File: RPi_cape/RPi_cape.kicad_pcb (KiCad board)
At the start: 4 copper layers, 104 x 255 mm, 505 parts, among them J1 Conn_01x04, J10 Conn_01x02, J11 Conn_01x02, J12 Conn_01x02, J13 Conn_01x02, J14 Conn_01x02, J16 Conn_01x06, J17 Pressure_sensor_barb, J18 Pressure_sensor_barb, J19 Pressure_sensor_barb, J2 Conn_01x02, J20 Pressure_sensor_barb, J3 Conn_01x02, J4 Conn_01x02, J5 Conn_01x03, J6 Conn_01x03, J7 Conn_01x02, J8 Conn_02x20_Odd_Even, J9 Conn_01x02, P15 Conn_02x05_Odd_Even, Q1 MMBT3904, Q10 MMBT3904, Q11 MMBT3904, Q12 MMBT3906, Q13 MMBT3904, Q5 MMBT3904, Q6 DNP, Q7 DNP, Q8 MMBT3904, Q9 MMBT3904, U1 TL431A, U10 MS5803-05BA, U11 LM2903, U12 LMC7101B, U13 LMC7101B, U14 BMP388, U15 MS5803-05BA, U16 BMP388, U17 LM2903, U18 74LVC1G08, U19 TPS1H100B, U2 ADC128D818, U20 74LVC1G08, U21 TPS1H100B, U22 74LVC1G08, U23 TPS1H100B, U24 TL431A, U25 LM2903, U26 MIC1557, U27 MIC1557, U28 LM4871M, U29 LP5907MFX-3.3, U3 ADC128D818, U30 LP5907MFX-1.8, U31 DNP (5M40ZE64), U32 MIC1557, U33 5M80ZT100 / 5M240ZT100, U34 LMZ14203, U35 LMZ14203, U36 LMC7101B, U37 LMC7101B, U38 LMC7101B, U4 AD8552A, U5 LM2903, U6 LMC7101B, U7 LMC7101B, U8 74LVC1G08, U9 TPS1H100B

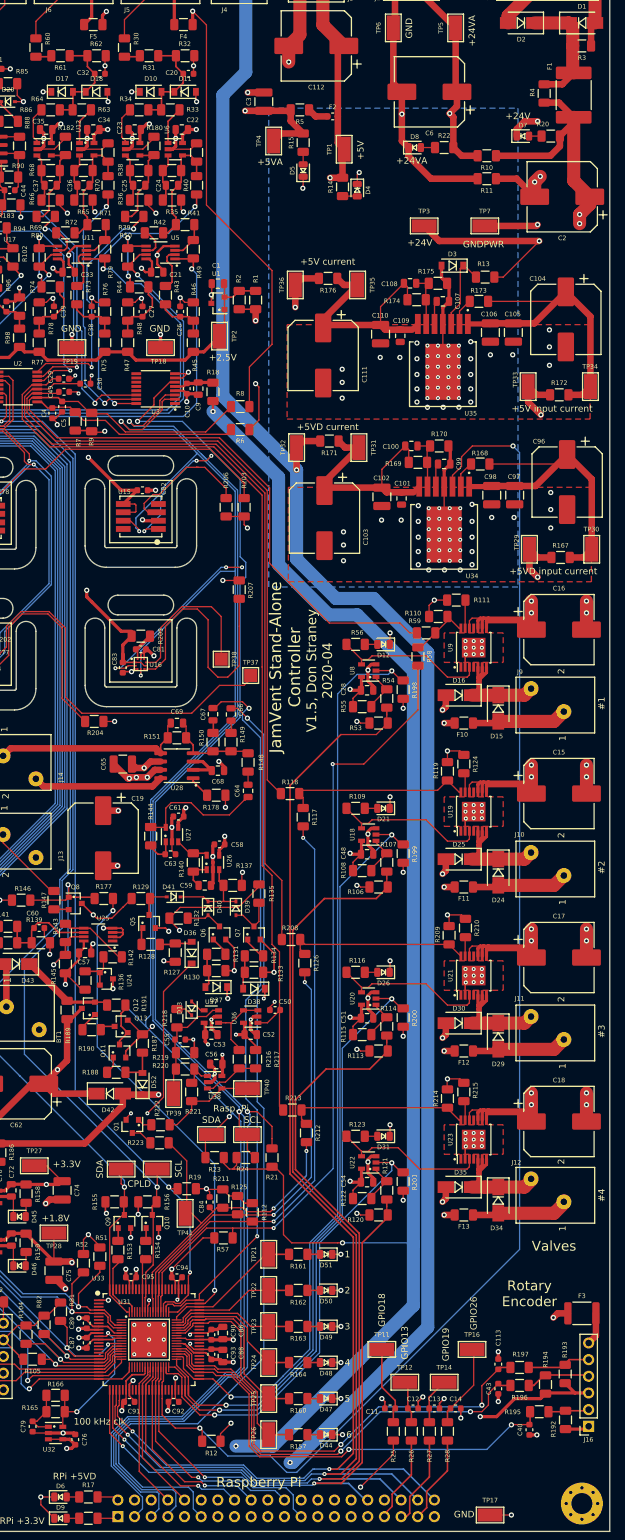
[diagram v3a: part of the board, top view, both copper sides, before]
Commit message: Safety additions
Switched CPLD_ADC7 to +24V monitoring (from +5V monitoring), and added CPLD ~Bat_On digital input(s) to know when it's running from backup battery, to cover low-input-voltage edge cases
Added series 1K resistors (R226-231) on CPLD<->RPi Comms1-6 lines, to protect CPLD in case of overvoltage from RPi failure
Added optional input TVS D23 to handle sustained over-voltage or large surges
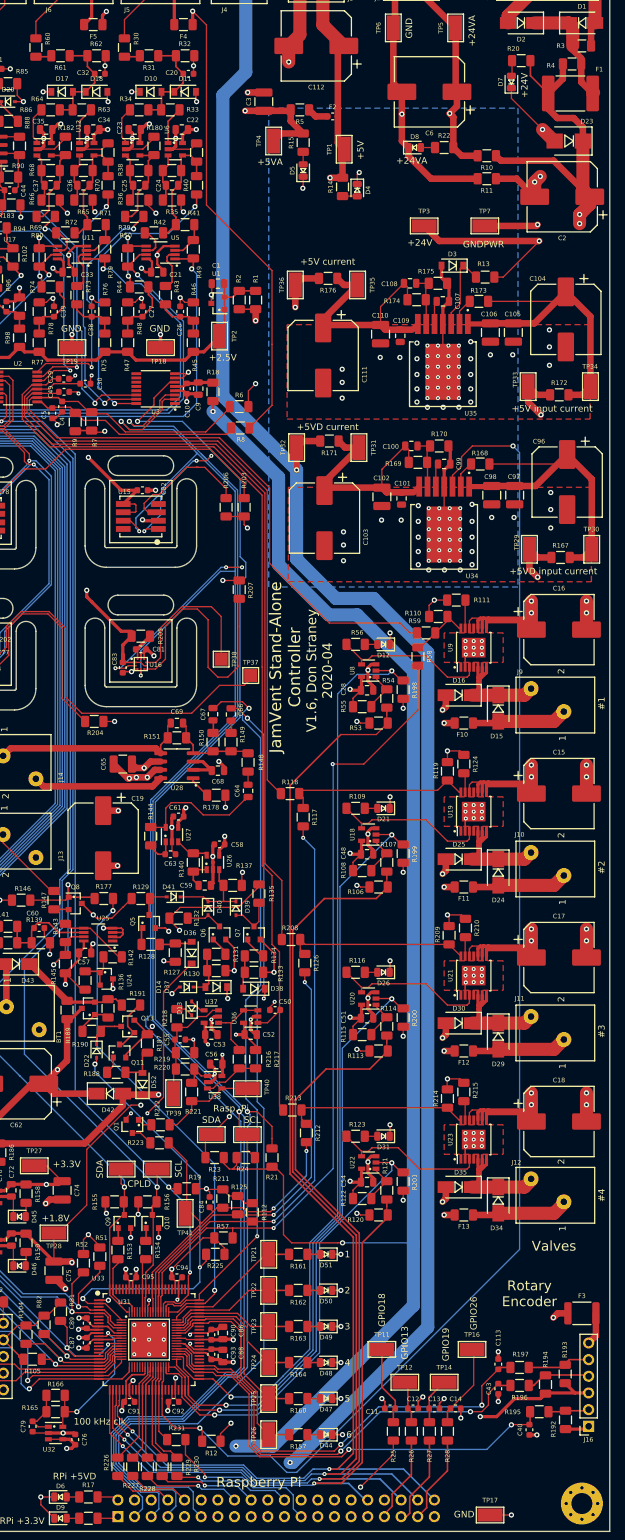
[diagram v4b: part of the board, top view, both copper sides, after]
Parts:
- added D14: BAS21AH, Ventilator:D_SOD-323, F.Cu at (68.0, 200.5)
- added D22: BAS21AH, Ventilator:D_SOD-323, F.Cu at (54.2, 210.2)
- added D23: DNP, Ventilator:D_SMB, F.Cu at (126.2, 71.5)
- added R224: 10K, Resistor_SMD:R_1206_3216Metric, F.Cu at (56.0, 203.8)
- added R225: 10K, Resistor_SMD:R_1206_3216Metric, F.Cu at (72.3, 241.2)
- added R226: 1K, Resistor_SMD:R_1206_3216Metric, F.Cu at (57.5, 273.6)
- added R227: 1K, Resistor_SMD:R_1206_3216Metric, F.Cu at (59.8, 273.6)
- added R228: 1K, Resistor_SMD:R_1206_3216Metric, F.Cu at (62.0, 273.6)
- added R229: 1K, Resistor_SMD:R_1206_3216Metric, F.Cu at (64.2, 273.6)
- added R230: 1K, Resistor_SMD:R_1206_3216Metric, F.Cu at (66.5, 273.6)
- added R231: 1K, Resistor_SMD:R_1206_3216Metric, F.Cu at (66.4, 269.5)
- D37: value 3.3V -> DNP (3.3V)
- D38: value 20V -> DNP (20V)
- D39: value BAS21AH -> DNP (BAS21AH)
- Q6: value DNP -> MMBT3904
- R130, R9: value DNP -> 1K
- R131, R132, R8: value DNP -> 10K
- R6, R7: value 10K -> DNP (10K)
- moved R20 12.3 mm to (119.0, 59.2)
- moved D7 8.43 mm to (117.5, 62.5), turned to 90 degrees
- moved R4 6.19 mm to (126.8, 59.8), turned to 180 degrees
- moved R6 3.50 mm to (76.0, 112.0)
- moved R8 3.25 mm to (76.2, 115.2)
- moved R7 2.50 mm to (53.5, 114.2)
- moved R9 2.50 mm to (51.0, 114.3)
- moved R191 2.25 mm to (59.5, 203.2)
- moved C4 1.80 mm to (49.0, 112.0)
- moved C5 1.80 mm to (47.5, 113.0)
- moved Q13 1.00 mm to (59.0, 206.5)
- moved R187 0.75 mm to (62.0, 209.1)
- moved F1 0.56 mm to (126.5, 64.2), turned to 0 degrees
- moved R190 0.25 mm to (53.5, 207.2)
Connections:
- C4 pad 2: /CPLD_ADC7 -> /CPLD_ADC6
- C5 pad 2: /CPLD_ADC6 -> /CPLD_ADC7
- R6 pad 2: /CPLD_ADC7 -> /CPLD_ADC6
- R7 pad 1: /CPLD_ADC7 -> /CPLD_ADC6
- R8 pad 2: /CPLD_ADC6 -> /CPLD_ADC7
- R9 pad 1: /CPLD_ADC6 -> /CPLD_ADC7
- U31 pad 1: Net-(U31-Pad1) -> /Auditory Alarm/~Bat_On
- U31 pad 24: /Comms1 -> /CPLD/Comms1
- U31 pad 25: /Comms2 -> /CPLD/Comms2
- U31 pad 26: /Comms3 -> /CPLD/Comms3
- U31 pad 27: /Comms4 -> /CPLD/Comms4
- U31 pad 28: /Comms5 -> /CPLD/Comms5
- U31 pad 29: /Comms6 -> /CPLD/Comms6
- U33 pad 2: Net-(U33-Pad2) -> /Auditory Alarm/~Bat_On
- U33 pad 35: /Comms1 -> /CPLD/Comms1
- U33 pad 36: /Comms2 -> /CPLD/Comms2
- U33 pad 37: /Comms3 -> /CPLD/Comms3
- U33 pad 39: /Comms4 -> /CPLD/Comms4
- U33 pad 40: /Comms5 -> /CPLD/Comms5
- U33 pad 41: /Comms6 -> /CPLD/Comms6
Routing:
- net /Auditory Alarm/~Bat_On: track 0.00 -> 70.0 mm, vias 0 -> 3
- net +1V8: track 72.4 -> 120.1 mm, vias 3 -> 5
- net /Comms5: track 34.8 -> 17.9 mm
- net /Comms4: track 31.0 -> 15.1 mm
- net /CPLD/Comms5: track 0.00 -> 15.9 mm
- net /CPLD/Comms1: track 0.00 -> 15.7 mm
- net +24V: track 225.0 -> 240.7 mm
- net /Comms3: track 29.9 -> 14.8 mm
- net /CPLD/Comms2: track 0.00 -> 14.9 mm
- net /CPLD/Comms4: track 0.00 -> 14.6 mm
- net /CPLD/Comms3: track 0.00 -> 14.4 mm
- net /Comms2: track 23.4 -> 9.48 mm
- net /Comms1: track 22.6 -> 9.14 mm
- net /Comms6: track 38.2 -> 25.4 mm
- net /CPLD/Comms6: track 0.00 -> 11.7 mm
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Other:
- board text added: "V1.6, Don Straney 2020-04"
- board text removed: "V1.5, Don Straney 2020-04"

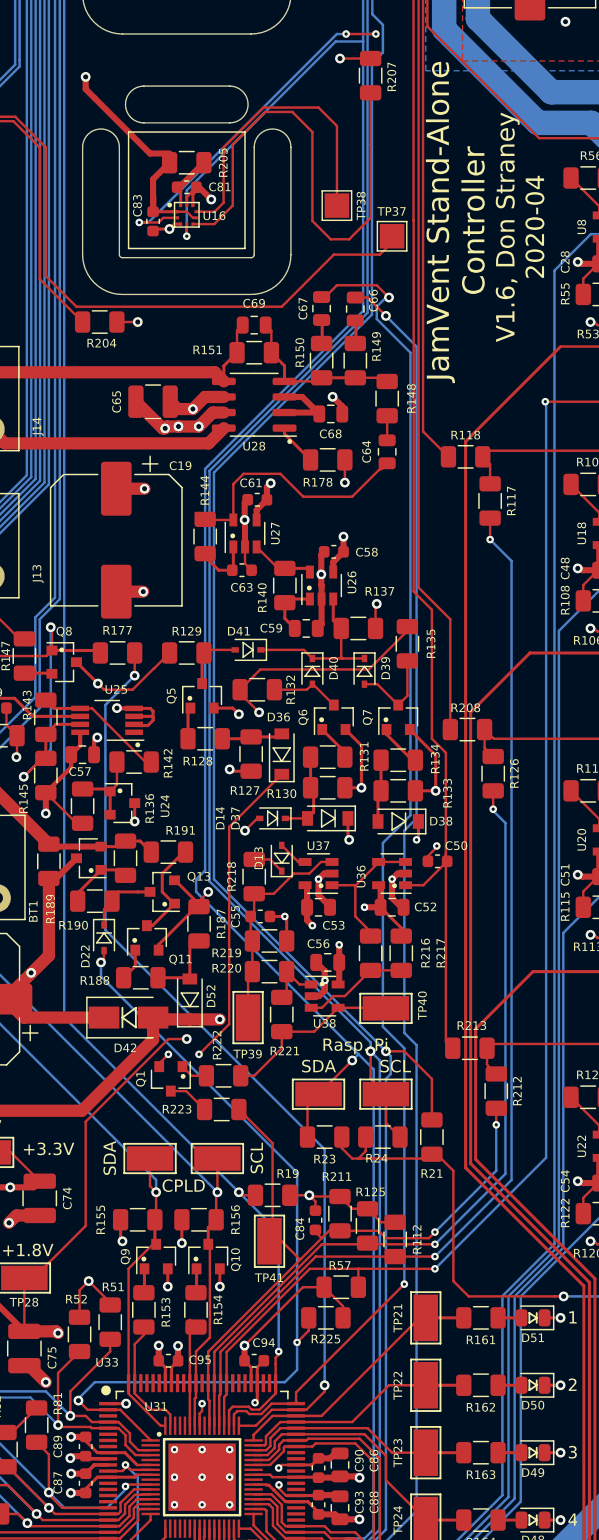
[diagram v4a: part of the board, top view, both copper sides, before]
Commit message: +5VA outage detection
Separated +1.8V and +5VA monitoring and added +3.3V output for +5VA on ~5VA_On signal to CPLD, to cover an extra failure mode
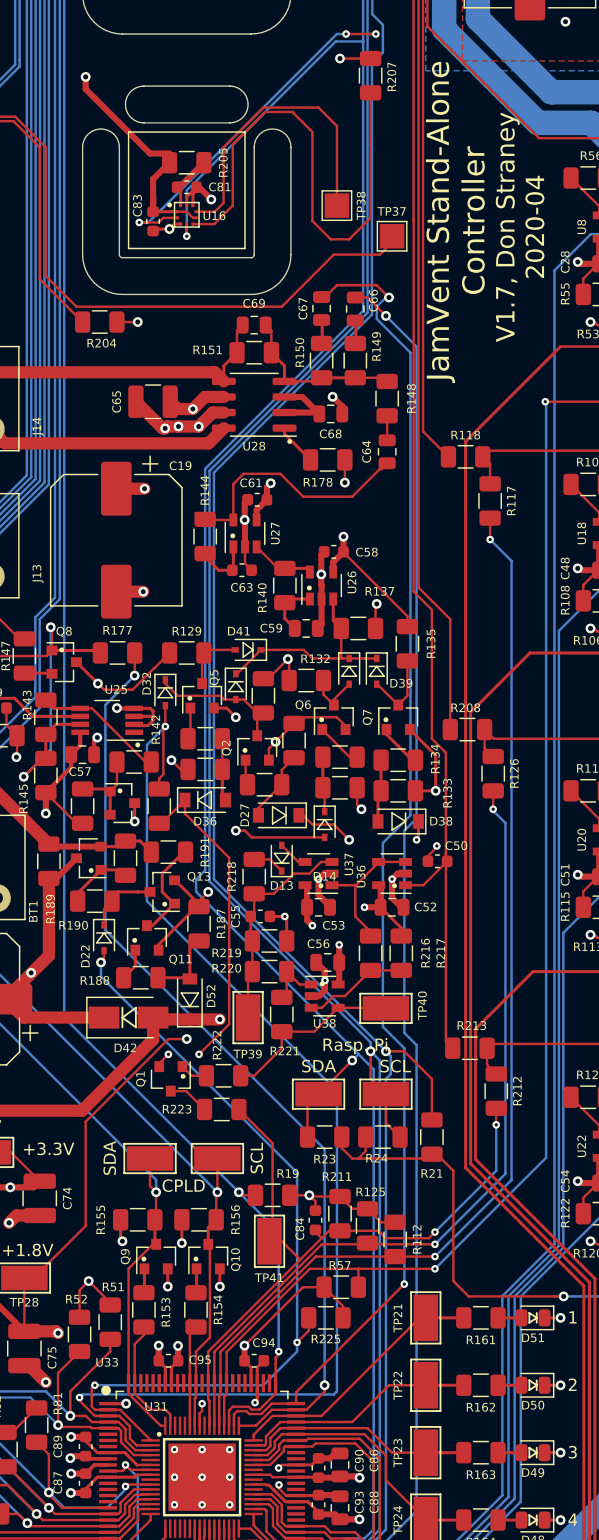
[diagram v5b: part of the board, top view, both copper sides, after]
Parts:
- removed D37: DNP (3.3V), Ventilator:D_SOD-123
- added D27: 3.3V, Ventilator:D_SOD-123, F.Cu at (68.5, 200.2)
- added D28: DNP (BAS21AH), Ventilator:D_SOD-323, F.Cu at (65.0, 189.8)
- added D32: BAS21AH, Ventilator:D_SOD-323, F.Cu at (59.2, 190.2)
- added Q2: MMBT3904, Ventilator:SOT-23, F.Cu at (66.8, 194.8)
- added R232: 10K, Resistor_SMD:R_1206_3216Metric, F.Cu at (69.8, 194.2)
- added R233: 10K, Resistor_SMD:R_1206_3216Metric, F.Cu at (67.3, 197.8)
- added R234: 10K, Resistor_SMD:R_1206_3216Metric, F.Cu at (67.2, 190.5)
- added R235: 10K, Resistor_SMD:R_1206_3216Metric, F.Cu at (58.8, 199.5)
- moved D36 7.29 mm to (62.5, 199.0), turned to 0 degrees
- moved D14 4.28 mm to (72.2, 201.0), turned to 270 degrees
- moved R132 4.07 mm to (70.8, 189.2)
- moved R127 3.95 mm to (62.5, 196.5), turned to 0 degrees
- moved D40 3.00 mm to (74.2, 188.5)
- moved D39 1.00 mm to (76.5, 188.5)
- moved R130 1.00 mm to (73.5, 198.0)
- moved R131 1.00 mm to (73.5, 195.5)
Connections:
- U31 pad 2: Net-(U31-Pad2) -> /Auditory Alarm/~+5VA_On
- U33 pad 3: Net-(U33-Pad3) -> /Auditory Alarm/~+5VA_On
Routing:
- net /Auditory Alarm/~+5VA_On: track 0.00 -> 97.8 mm, vias 0 -> 2
- net Net-(D28-Pad2): track 0.00 -> 10.6 mm
- net +1V8: track 120.1 -> 126.7 mm
- net Net-(D27-Pad2): track 0.00 -> 5.90 mm
- net +BATT: track 96.2 -> 91.6 mm
- net GND: track 555.3 -> 559.1 mm, vias 274 -> 275
- net Net-(D28-Pad1): track 13.9 -> 17.7 mm
- net +5VA: track 181.8 -> 185.0 mm
- net /Auditory Alarm/~Bat_On: track 70.0 -> 67.5 mm
- net Net-(Q2-Pad1): track 0.00 -> 2.06 mm
- net Net-(D14-Pad1): track 7.01 -> 5.06 mm
- net Net-(D40-Pad2): track 5.74 -> 4.57 mm
- net Net-(D39-Pad2): track 7.36 -> 6.31 mm
- net Net-(Q6-Pad1): track 3.12 -> 3.93 mm
- net Net-(D41-Pad2): track 4.65 -> 5.22 mm
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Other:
- board text added: "V1.7, Don Straney 2020-04"
- board text removed: "V1.6, Don Straney 2020-04"
